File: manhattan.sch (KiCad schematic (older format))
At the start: 111 parts, among them J1 USB, J2 MICROSD-JT10, K1 CONN_3, K2 CONN_3, K3 CONN_3, K4 CONN_3, P1 CONN_2, P2 CONN_2, P3 CONN_2, P4 CONN_6, P5 CONN_7X2, Q1 MOSFET_N, Q2 MOSFET_N, Q3 MOSFET_N, U1 MC78M05CDTX, U2 AP7313, U3 TXB0104, X1 16.000

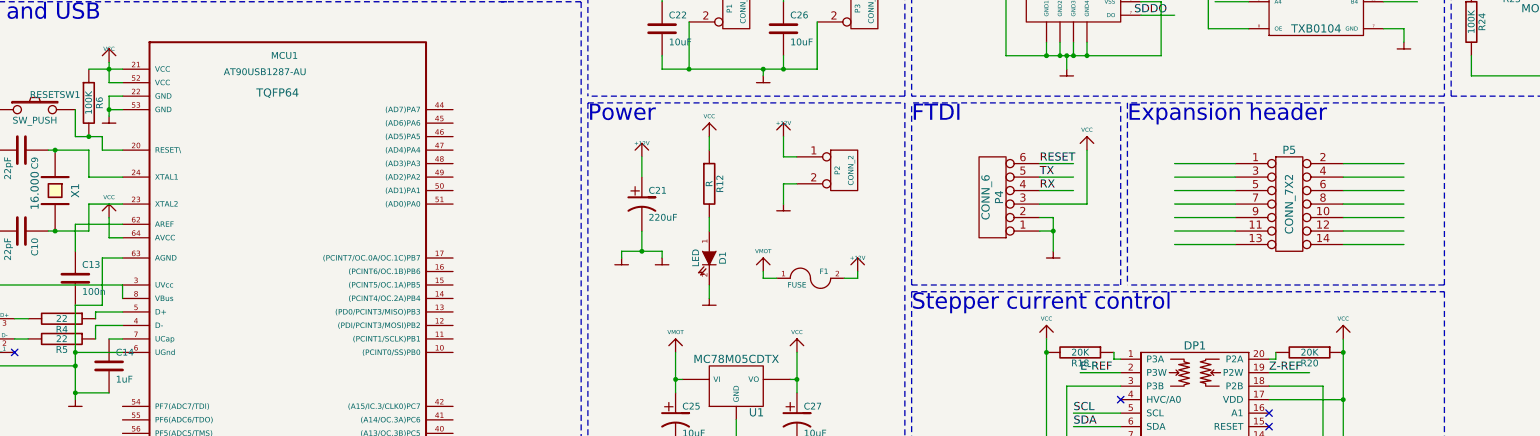
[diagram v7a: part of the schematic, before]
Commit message: Remove FTDI header and add ICSP
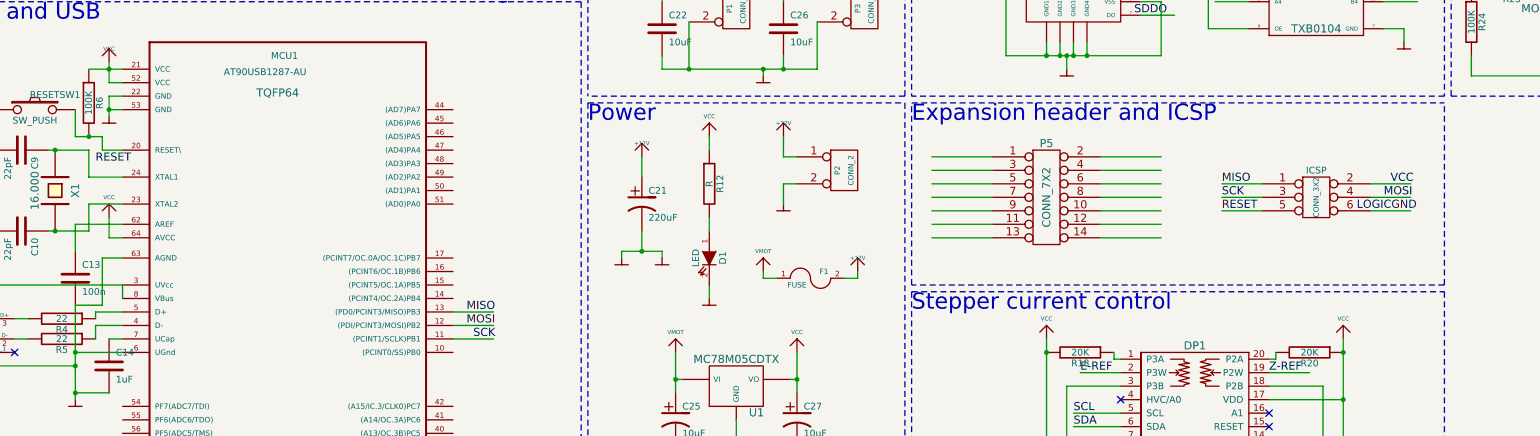
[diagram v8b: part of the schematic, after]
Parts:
- removed P4: CONN_6, symbol CONN_6
- added ICSP: CONN_3X2, symbol CONN_3X2
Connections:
- net labels added: SCK
- wire segments 465 -> 466
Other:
- note added: "Expansion header and ICSP"
- note removed: "Expansion header"
- note removed: "FTDI"
- moved on the sheet: P5
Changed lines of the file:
@@
-EESchema Schematic File Version 2  date Thu 15 Mar 2012 04:26:36 PM EDT
+EESchema Schematic File Version 2  date Tue 20 Mar 2012 10:49:40 AM EDT
 LIBS:manhattan
 LIBS:power
@@
 Sheet 1 1
 Title ""
-Date "15 mar 2012"
+Date "20 mar 2012"
 Rev ""
 Comp ""
@@
 Comment4 ""
 $EndDescr
-NoConn ~ 11200 8350
-NoConn ~ 10100 8150
-NoConn ~ 11200 8250
+Text Label 5300 7700 0    60   ~ 0
+SCK
+Text Label 5250 7600 0    60   ~ 0
+MOSI
+Text Label 5250 7500 0    60   ~ 0
+MISO
+Wire Wire Line
+	5450 7700 5150 7700
+Wire Wire Line
+	5450 7500 5150 7500
+Wire Wire Line
+	12250 6650 11950 6650
+Wire Wire Line
+	10850 6750 11150 6750
+Wire Wire Line
+	10850 6550 11150 6550
 Wire Wire Line
 	9750 8250 10100 8250
@@
 	9700 8050 10100 8050
 Wire Notes Line
-	12500 7300 10150 7300
-Wire Notes Line
 	12500 7300 12500 5950
-Wire Notes Line
-	12500 5950 10150 5950
 Wire Notes Line
 	8500 5900 6150 5900
@@
 	14800 5750 14800 5300
 Connection ~ 14800 5750
-Wire Notes Line
-	10150 5950 10150 7300
-Wire Wire Line
-	12200 6900 11750 6900
-Wire Wire Line
-	12200 6700 11750 6700
-Wire Wire Line
-	12200 6500 11750 6500
-Wire Wire Line
-	10500 7000 10950 7000
-Wire Wire Line
-	10500 6800 10950 6800
-Wire Wire Line
-	10500 6600 10950 6600
-Wire Wire Line
-	10500 6400 10950 6400
+Wire Wire Line
+	10400 6850 9950 6850
+Wire Wire Line
+	10400 6650 9950 6650
+Wire Wire Line
+	10400 6450 9950 6450
+Wire Wire Line
+	8700 6950 9150 6950
+Wire Wire Line
+	8700 6750 9150 6750
+Wire Wire Line
+	8700 6550 9150 6550
+Wire Wire Line
+	8700 6350 9150 6350
 Wire Wire Line
 	5400 9800 5150 9800
-Wire Wire Line
-	9750 6600 9500 6600
-Wire Wire Line
-	9750 6500 9500 6500
-Wire Wire Line
-	9600 6900 9500 6900
 Connection ~ 15050 5750
 Wire Wire Line
@@
 	16450 4100 12550 4100
 Wire Wire Line
-	9500 6800 9600 6800
-Wire Wire Line
-	9600 6800 9600 7050
-Connection ~ 9600 6900
-Wire Wire Line
-	9750 6400 9500 6400
-Wire Wire Line
-	9500 6700 9850 6700
-Wire Wire Line
-	9850 6700 9850 6300
-Wire Wire Line
 	5400 9700 5150 9700
-Wire Notes Line
-	8550 7300 8550 5950
-Wire Notes Line
-	8550 7300 10100 7300
-Wire Notes Line
-	10100 7300 10100 5950
-Wire Notes Line
-	10100 5950 8550 5950
-Wire Wire Line
-	10500 6500 10950 6500
-Wire Wire Line
-	10500 6700 10950 6700
-Wire Wire Line
-	10500 6900 10950 6900
-Wire Wire Line
-	12200 6400 11750 6400
-Wire Wire Line
-	12200 6600 11750 6600
-Wire Wire Line
-	12200 6800 11750 6800
-Wire Wire Line
-	12200 7000 11750 7000
+Wire Wire Line
+	8700 6450 9150 6450
+Wire Wire Line
+	8700 6650 9150 6650
+Wire Wire Line
+	8700 6850 9150 6850
+Wire Wire Line
+	10400 6350 9950 6350
+Wire Wire Line
+	10400 6550 9950 6550
+Wire Wire Line
+	10400 6750 9950 6750
+Wire Wire Line
+	10400 6950 9950 6950
 Wire Wire Line
 	14750 4550 14800 4550
@@
 Wire Wire Line
 	9750 8350 10100 8350
+Wire Notes Line
+	12500 7300 8550 7300
+Wire Notes Line
+	8550 7300 8550 5950
+Wire Notes Line
+	8550 5950 12500 5950
+Wire Wire Line
+	10850 6650 11150 6650
+Wire Wire Line
+	12250 6550 11950 6550
+Wire Wire Line
+	12250 6750 11950 6750
+Wire Wire Line
+	5450 7600 5150 7600
+Text Label 2500 6400 0    60   ~ 0
+RESET
+Text Label 11850 6750 0    60   ~ 0
+LOGICGND
+Text Label 12050 6650 0    60   ~ 0
+MOSI
+Text Label 12100 6550 0    60   ~ 0
+VCC
+Text Label 10850 6750 0    60   ~ 0
+RESET
+Text Label 10850 6650 0    60   ~ 0
+SCK
+Text Label 10850 6550 0    60   ~ 0
+MISO
+$Comp
+L CONN_3X2 ICSP
+U 1 1 4F689823
+P 11550 6700
+F 0 "ICSP" H 11550 6950 50  0000 C CNN
+F 1 "CONN_3X2" V 11550 6750 40  0000 C CNN
+	1    11550 6700
+	1    0    0    -1
+$EndComp
+Text Notes 8550 6100 0    120  ~ 0
+Expansion header and ICSP
+NoConn ~ 11200 8350
+NoConn ~ 10100 8150
+NoConn ~ 11200 8250
 NoConn ~ 11200 8450
 Text Label 9750 8350 0    60   ~ 0
@@
 Text Notes 8550 7500 0    120  ~ 0
 Stepper current control
-Text Notes 10150 6100 0    120  ~ 0
-Expansion header
 $Comp
 L CONN_7X2 P5
 U 1 1 4F5BC3D9
-P 11350 6700
-F 0 "P5" H 11350 7100 60  0000 C CNN
-F 1 "CONN_7X2" V 11350 6700 60  0000 C CNN
-	1    11350 6700
-	1    0    0    -1
-$EndComp
-Text Notes 8550 6100 0    120  ~ 0
-FTDI
+P 9550 6650
+F 0 "P5" H 9550 7050 60  0000 C CNN
+F 1 "CONN_7X2" V 9550 6650 60  0000 C CNN
+	1    9550 6650
+	1    0    0    -1
+$EndComp
 Text Label 5150 9800 0    60   ~ 0
 RX
 Text Label 5150 9700 0    60   ~ 0
 TX
-Text Label 9500 6600 0    60   ~ 0
-RX
-Text Label 9500 6400 0    60   ~ 0
-RESET
-Text Label 9500 6500 0    60   ~ 0
-TX
-$Comp
-L VCC #PWR012
-U 1 1 4F5BB50E
-P 9850 6300
-F 0 "#PWR012" H 9850 6450 30  0001 C CNN
-F 1 "VCC" H 9850 6450 30  0000 C CNN
-	1    9850 6300
-	1    0    0    -1
-$EndComp
-$Comp
-L LOGICGND #PWR013
-U 1 1 4F5BB4F6
-P 9600 7100
-F 0 "#PWR013" H 9600 7100 30  0001 C CNN
-F 1 "LOGICGND" H 9600 7030 30  0001 C CNN
-	1    9600 7100
-	1    0    0    -1
-$EndComp
-$Comp
-L CONN_6 P4
-U 1 1 4F5BB4F1
-P 9150 6650
-F 0 "P4" V 9100 6650 60  0000 C CNN
-F 1 "CONN_6" V 9200 6650 60  0000 C CNN
-	1    9150 6650
-	-1   0    0    1
-$EndComp
 Text Notes 12550 4250 0    120  ~ 0
 MOSFETs
